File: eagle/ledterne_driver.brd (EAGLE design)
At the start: 24.3 x 23.1 mm, 15 parts, among them IC1 MEGA8-AI

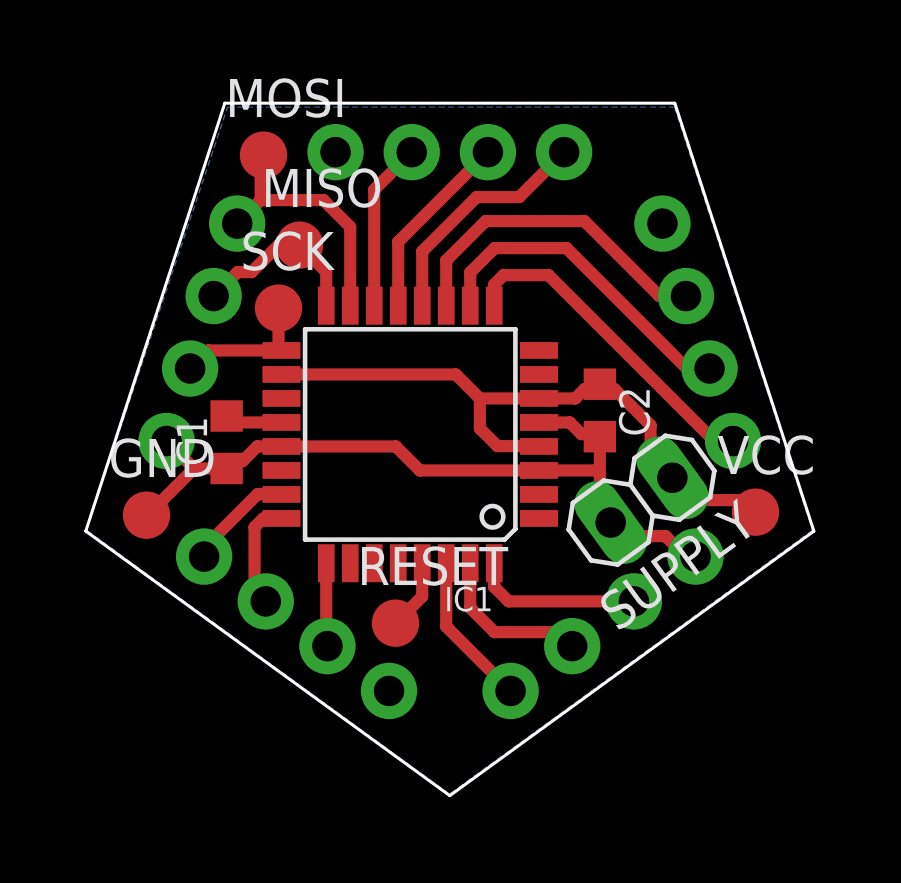
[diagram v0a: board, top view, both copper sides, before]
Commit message: Move MOSI solder pad away from board's corner
We might need this place for an additional mount.
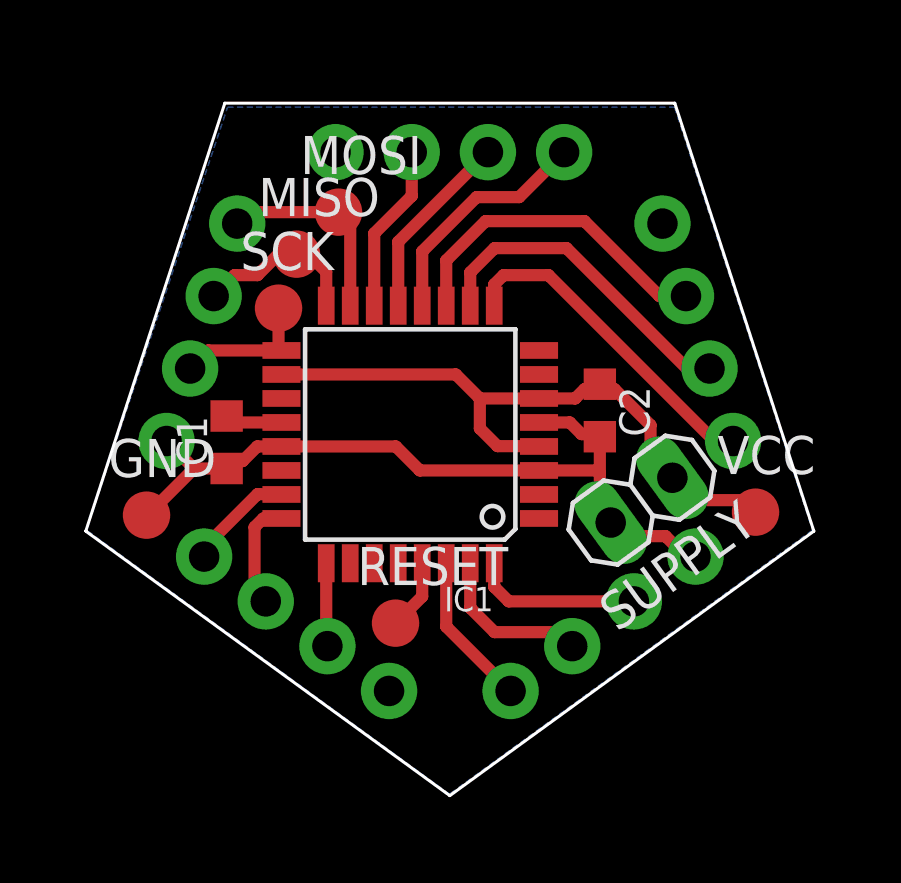
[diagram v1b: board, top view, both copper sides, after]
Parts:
- moved MOSI 3.14 mm to (12.8, 23.2)
- moved MISO 0.32 mm to (11.4, 21.8)
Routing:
- net MOSI: track 8.63 -> 6.81 mm
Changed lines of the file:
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@@
 <element name="GND" library="solpad-smd" package="SOLPAD-SMD" value="SOLPAD-SMD-NORMAL" x="6.4" y="13.1"/>
 <element name="SCK" library="solpad-smd" package="SOLPAD-SMD" value="SOLPAD-SMD-NORMAL" x="10.8" y="20"/>
-<element name="MISO" library="solpad-smd" package="SOLPAD-SMD" value="SOLPAD-SMD-NORMAL" x="11.5" y="22.1"/>
-<element name="MOSI" library="solpad-smd" package="SOLPAD-SMD" value="SOLPAD-SMD-NORMAL" x="10.3" y="25.1"/>
+<element name="MISO" library="solpad-smd" package="SOLPAD-SMD" value="SOLPAD-SMD-NORMAL" x="11.4" y="21.8"/>
+<element name="MOSI" library="solpad-smd" package="SOLPAD-SMD" value="SOLPAD-SMD-NORMAL" x="12.8" y="23.2"/>
 <element name="RESET" library="solpad-smd" package="SOLPAD-SMD" value="SOLPAD-SMD-NORMAL" x="14.7" y="9.5"/>
 <element name="VCC" library="solpad-smd" package="SOLPAD-SMD" value="SOLPAD-SMD-NORMAL" x="26.7" y="13.2"/>
@@
 <contactref element="IC1" pad="15"/>
 <contactref element="JP5" pad="1"/>
-<wire x1="13.19" y1="22.71" x2="13.19" y2="20.0826" width="0.4064" layer="1"/>
 <contactref element="MOSI" pad="MP"/>
-<wire x1="13.19" y1="22.71" x2="12.3" y2="23.6" width="0.4064" layer="1"/>
-<wire x1="12.3" y1="23.6" x2="10.203790625" y2="23.6" width="0.4064" layer="1"/>
-<wire x1="10.203790625" y1="23.6" x2="9.422671875" y2="22.81888125" width="0.4064" layer="1"/>
-<wire x1="10.203790625" y1="23.6" x2="10.203790625" y2="25.003790625" width="0.4064" layer="1"/>
-<wire x1="10.203790625" y1="25.003790625" x2="10.3" y2="25.1" width="0.4064" layer="1"/>
+<wire x1="12.8" y1="23.2" x2="9.803790625" y2="23.2" width="0.4064" layer="1"/>
+<wire x1="9.803790625" y1="23.2" x2="9.422671875" y2="22.81888125" width="0.4064" layer="1"/>
+<wire x1="13.19" y1="20.0826" x2="13.19" y2="22.81" width="0.4064" layer="1"/>
+<wire x1="13.19" y1="22.81" x2="12.8" y2="23.2" width="0.4064" layer="1"/>
 </signal>
 <signal name="MISO">
@@
 <contactref element="MISO" pad="MP"/>
 <wire x1="12.39" y1="20.0826" x2="12.39" y2="21.21" width="0.4064" layer="1"/>
-<wire x1="12.39" y1="21.21" x2="11.5" y2="22.1" width="0.4064" layer="1"/>
-<wire x1="11.5" y1="22.1" x2="10.8" y2="22.1" width="0.4064" layer="1"/>
-<wire x1="10.8" y1="22.1" x2="9.9" y2="21.2" width="0.4064" layer="1"/>
-<wire x1="9.9" y1="21.2" x2="9.434575" y2="21.2" width="0.4064" layer="1"/>
-<wire x1="9.434575" y1="21.2" x2="8.637771875" y2="20.403196875" width="0.4064" layer="1"/>
+<wire x1="12.39" y1="21.21" x2="11.8" y2="21.8" width="0.4064" layer="1"/>
+<wire x1="11.8" y1="21.8" x2="11.4" y2="21.8" width="0.4064" layer="1"/>
+<wire x1="11.4" y1="21.8" x2="10.8" y2="21.8" width="0.4064" layer="1"/>
+<wire x1="10.8" y1="21.8" x2="10.1" y2="21.1" width="0.4064" layer="1"/>
+<wire x1="10.1" y1="21.1" x2="9.334575" y2="21.1" width="0.4064" layer="1"/>
+<wire x1="9.334575" y1="21.1" x2="8.637771875" y2="20.403196875" width="0.4064" layer="1"/>
 </signal>
 <signal name="SCK">
@@
 <contactref element="IC1" pad="14"/>
 <contactref element="JP1" pad="3"/>
-<wire x1="15.24" y1="25.2" x2="13.99" y2="23.95" width="0.4064" layer="1"/>
-<wire x1="13.99" y1="23.95" x2="13.99" y2="20.0826" width="0.4064" layer="1"/>
+<wire x1="13.99" y1="22.49" x2="13.99" y2="20.0826" width="0.4064" layer="1"/>
+<wire x1="13.99" y1="22.49" x2="15.24" y2="23.74" width="0.4064" layer="1"/>
+<wire x1="15.24" y1="23.74" x2="15.24" y2="25.2" width="0.4064" layer="1"/>
 </signal>
 <signal name="N$4">

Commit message: Add capacitor values
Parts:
- C1, C2: value (none) -> 100n
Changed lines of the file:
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@@
 <attribute name="MPN" value="ATMEGA8-16AU" x="15.19" y="15.79" size="1.778" layer="27" rot="R180" display="off"/>
 </element>
-<element name="C1" library="rcl" package="C0603K" value="" x="9.07" y="15.53" rot="R90"/>
-<element name="C2" library="rcl" package="C0603K" value="" x="21.51" y="16.59" rot="R270"/>
+<element name="C1" library="rcl" package="C0603K" value="100n" x="9.07" y="15.53" rot="R90"/>
+<element name="C2" library="rcl" package="C0603K" value="100n" x="21.51" y="16.59" rot="R270"/>
 <element name="JP1" library="pinhead_round_pads" package="1X04/90" value="" x="16.51" y="29.01" rot="MR0"/>
 <element name="JP2" library="pinhead_round_pads" package="1X04/90" value="" x="28.39820625" y="20.3727125" rot="MR72"/>

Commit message: Clean up the schematic a little
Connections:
- removed net N$14: IC1.8
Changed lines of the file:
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@@
 <wire x1="9.385" y1="16.19" x2="9.07" y2="16.405" width="0.4064" layer="1"/>
-</signal>
-<signal name="N$14">
-<contactref element="IC1" pad="8"/>
 </signal>
 <signal name="N$3">

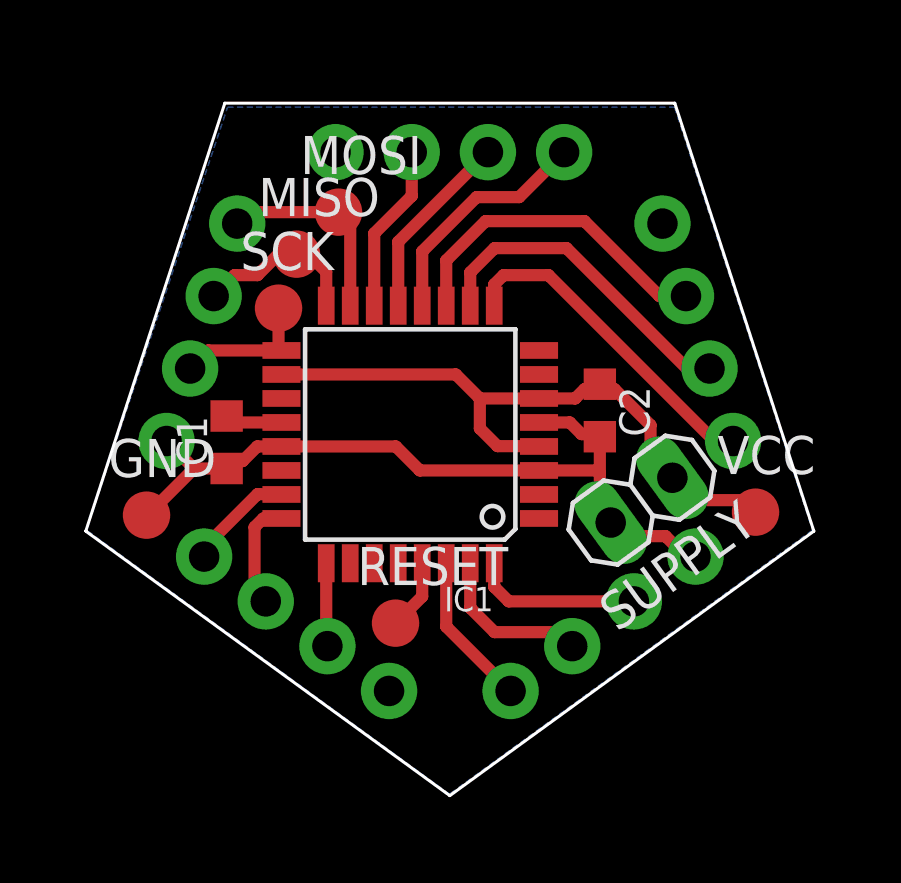
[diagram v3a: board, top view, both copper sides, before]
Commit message: Increase driver board's side length to 16 mm
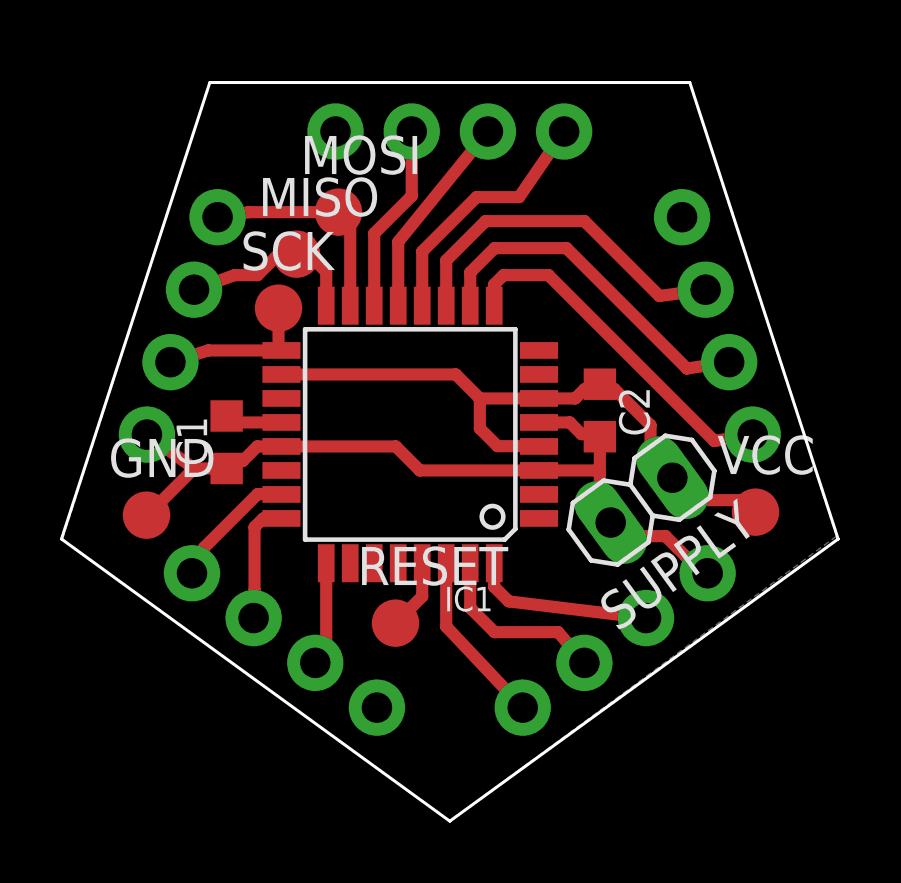
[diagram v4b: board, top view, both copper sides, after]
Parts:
- moved JP1 0.69 mm to (16.5, 29.7)
- moved JP5 0.69 mm to (3.97, 20.6)
- moved JP2 0.69 mm to (29.1, 20.6)
- moved JP3 0.69 mm to (24.3, 5.84)
- moved JP4 0.69 mm to (8.76, 5.84)
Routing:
- net GND: track 26.3 -> 27.5 mm
- net N$3: track 5.64 -> 6.32 mm
- net N$10: track 5.42 -> 6.10 mm
- net N$9: track 5.15 -> 5.83 mm
- net N$8: track 11.1 -> 11.8 mm
- net N$7: track 11.1 -> 11.8 mm
- net N$6: track 11.1 -> 11.7 mm
- net N$12: track 3.62 -> 4.27 mm
- net N$15: track 2.78 -> 3.42 mm
- net N$5: track 7.91 -> 8.44 mm
- net N$4: track 6.36 -> 6.87 mm
- net MOSI: track 6.81 -> 7.32 mm
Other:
- board size 24.3 x 23.1 mm -> 25.9 x 24.6 mm
- board text added: "16 mm"
- board text removed: "15 mm"

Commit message: Replace ISP solder pads with through-hole pins
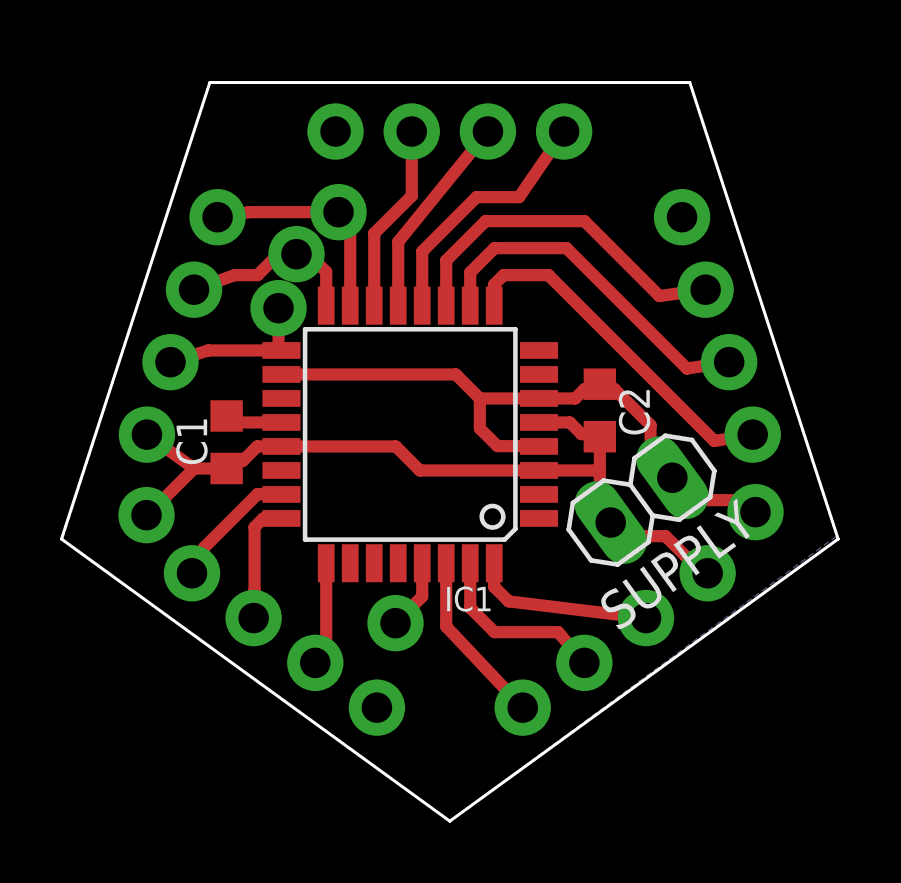
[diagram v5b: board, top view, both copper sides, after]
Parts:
- GND, MISO, MOSI, RESET, SCK, VCC: value SOLPAD-SMD-NORMAL -> LSP10; device solpad-smd:SOLPAD-SMD -> solpad-ledterne:LSP10
- flipped GND to the bottom
- flipped MISO to the bottom
- flipped MOSI to the bottom
- flipped RESET to the bottom
- flipped SCK to the bottom
- flipped VCC to the bottom
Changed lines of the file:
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@@
 <element name="JP5" library="pinhead_round_pads" package="1X04/90" value="" x="3.96731875" y="20.5853625" rot="MR288"/>
 <element name="SUPPLY" library="pinhead" package="1X02" value="" x="22.9" y="13.6" rot="R216"/>
-<element name="GND" library="solpad-smd" package="SOLPAD-SMD" value="SOLPAD-SMD-NORMAL" x="6.4" y="13.1"/>
-<element name="SCK" library="solpad-smd" package="SOLPAD-SMD" value="SOLPAD-SMD-NORMAL" x="10.8" y="20"/>
-<element name="MISO" library="solpad-smd" package="SOLPAD-SMD" value="SOLPAD-SMD-NORMAL" x="11.4" y="21.8"/>
-<element name="MOSI" library="solpad-smd" package="SOLPAD-SMD" value="SOLPAD-SMD-NORMAL" x="12.8" y="23.2"/>
-<element name="RESET" library="solpad-smd" package="SOLPAD-SMD" value="SOLPAD-SMD-NORMAL" x="14.7" y="9.5"/>
-<element name="VCC" library="solpad-smd" package="SOLPAD-SMD" value="SOLPAD-SMD-NORMAL" x="26.7" y="13.2"/>
+<element name="RESET" library="solpad-ledterne" package="LSP10" value="LSP10" x="14.7" y="9.5" rot="MR0"/>
+<element name="VCC" library="solpad-ledterne" package="LSP10" value="LSP10" x="26.7" y="13.2" rot="MR0"/>
+<element name="GND" library="solpad-ledterne" package="LSP10" value="LSP10" x="6.4" y="13.1" rot="MR0"/>
+<element name="MISO" library="solpad-ledterne" package="LSP10" value="LSP10" x="11.4" y="21.8" rot="MR0"/>
+<element name="SCK" library="solpad-ledterne" package="LSP10" value="LSP10" x="10.8" y="20" rot="MR0"/>
+<element name="MOSI" library="solpad-ledterne" package="LSP10" value="LSP10" x="12.8" y="23.2" rot="MR0"/>
 </elements>
 <signals>
@@
 <wire x1="9.6" y1="14.9" x2="9.315" y2="14.9" width="0.4064" layer="1"/>
 <wire x1="9.315" y1="14.9" x2="9.07" y2="14.655" width="0.4064" layer="1"/>
-<contactref element="GND" pad="MP"/>
 <wire x1="6.4" y1="13.1" x2="6.429796875" y2="13.1" width="0.4064" layer="1"/>
 <wire x1="6.429796875" y1="13.1" x2="7.984796875" y2="14.655" width="0.4064" layer="1"/>
@@
 <vertex x="3.6" y="12.3"/>
 </polygon>
+<contactref element="GND" pad="MP"/>
+<wire x1="12.7" y1="25.88815625" x2="10.8974" y2="15.39" width="0" layer="19" extent="1-1"/>
 </signal>
 <signal name="VCC">
@@
 <wire x1="23.2" y1="16.1" x2="23.2" y2="15.073934375" width="0.4064" layer="1"/>
 <wire x1="23.2" y1="15.073934375" x2="23.92745" y2="14.346484375" width="0.4064" layer="1"/>
-<contactref element="VCC" pad="MP"/>
 <wire x1="24.673934375" y1="13.6" x2="26.3" y2="13.6" width="0.4064" layer="1"/>
 <wire x1="26.3" y1="13.6" x2="26.7" y2="13.2" width="0.4064" layer="1"/>
 <wire x1="24.673934375" y1="13.6" x2="23.92745" y2="14.346484375" width="0.4064" layer="1"/>
+<contactref element="VCC" pad="MP"/>
 </signal>
 <signal name="RESET">
 <contactref element="IC1" pad="29"/>
-<contactref element="RESET" pad="MP"/>
 <wire x1="15.59" y1="11.4974" x2="15.59" y2="10.39" width="0.4064" layer="1"/>
 <wire x1="15.59" y1="10.39" x2="14.7" y2="9.5" width="0.4064" layer="1"/>
+<contactref element="RESET" pad="MP"/>
 </signal>
 <signal name="MOSI">
 <contactref element="IC1" pad="15"/>
 <contactref element="JP5" pad="1"/>
-<contactref element="MOSI" pad="MP"/>
 <wire x1="12.8" y1="23.2" x2="9.803790625" y2="23.2" width="0.4064" layer="1"/>
 <wire x1="9.803790625" y1="23.2" x2="8.768196875" y2="23.03153125" width="0.4064" layer="1"/>
 <wire x1="13.19" y1="20.0826" x2="13.19" y2="22.81" width="0.4064" layer="1"/>
 <wire x1="13.19" y1="22.81" x2="12.8" y2="23.2" width="0.4064" layer="1"/>
+<contactref element="MOSI" pad="MP"/>
 </signal>
 <signal name="MISO">
 <contactref element="IC1" pad="16"/>
 <contactref element="JP5" pad="2"/>
-<contactref element="MISO" pad="MP"/>
 <wire x1="12.39" y1="20.0826" x2="12.39" y2="21.21" width="0.4064" layer="1"/>
 <wire x1="12.39" y1="21.21" x2="11.8" y2="21.8" width="0.4064" layer="1"/>
@@
 <wire x1="10.1" y1="21.1" x2="9.334575" y2="21.1" width="0.4064" layer="1"/>
 <wire x1="9.334575" y1="21.1" x2="7.98329375" y2="20.615846875" width="0.4064" layer="1"/>
+<contactref element="MISO" pad="MP"/>
 </signal>
 <signal name="SCK">
@@
 <contactref element="JP5" pad="3"/>
 <wire x1="7.19839375" y1="18.200165625" x2="8.455353125" y2="18.59" width="0.4064" layer="1"/>
-<wire x1="8.455353125" y1="18.59" x2="10.8974" y2="18.59" width="0.4064" layer="1"/>
-<contactref element="SCK" pad="MP"/>
+<wire x1="8.455353125" y1="18.59" x2="10.8" y2="18.59" width="0.4064" layer="1"/>
 <wire x1="10.8974" y1="18.59" x2="10.8" y2="18.59" width="0.4064" layer="1"/>
 <wire x1="10.8" y1="18.59" x2="10.8" y2="20" width="0.4064" layer="1"/>
+<contactref element="SCK" pad="MP"/>
 </signal>
 <signal name="N$1">
